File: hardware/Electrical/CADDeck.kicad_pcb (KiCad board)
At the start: 2 copper layers, 129 x 82.1 mm, 26 parts, among them J1 Conn_01x05_Socket, J4 Conn_01x04_Socket, J5 Conn_01x10_Socket, SW1 SW_Push, SW10 SW_Push, SW2 SW_Push, SW3 SW_Push, SW4 SW_Push, SW5 SW_Push, SW6 SW_Push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

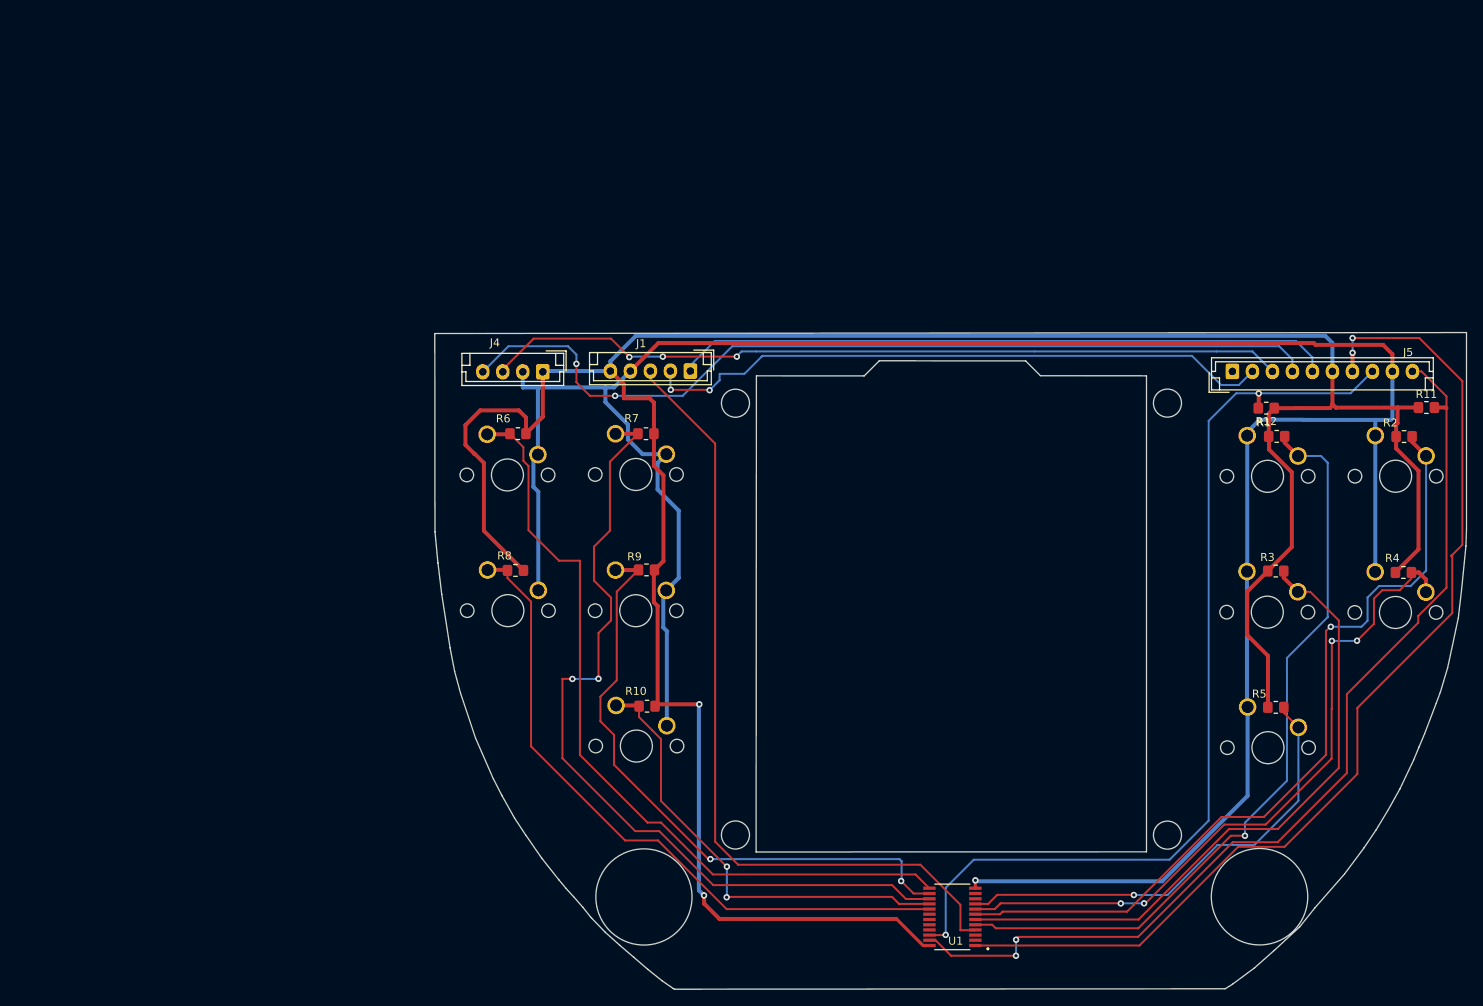
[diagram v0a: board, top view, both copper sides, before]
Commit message: Platine aktualisiert
LED Beleuchtung für Tasten
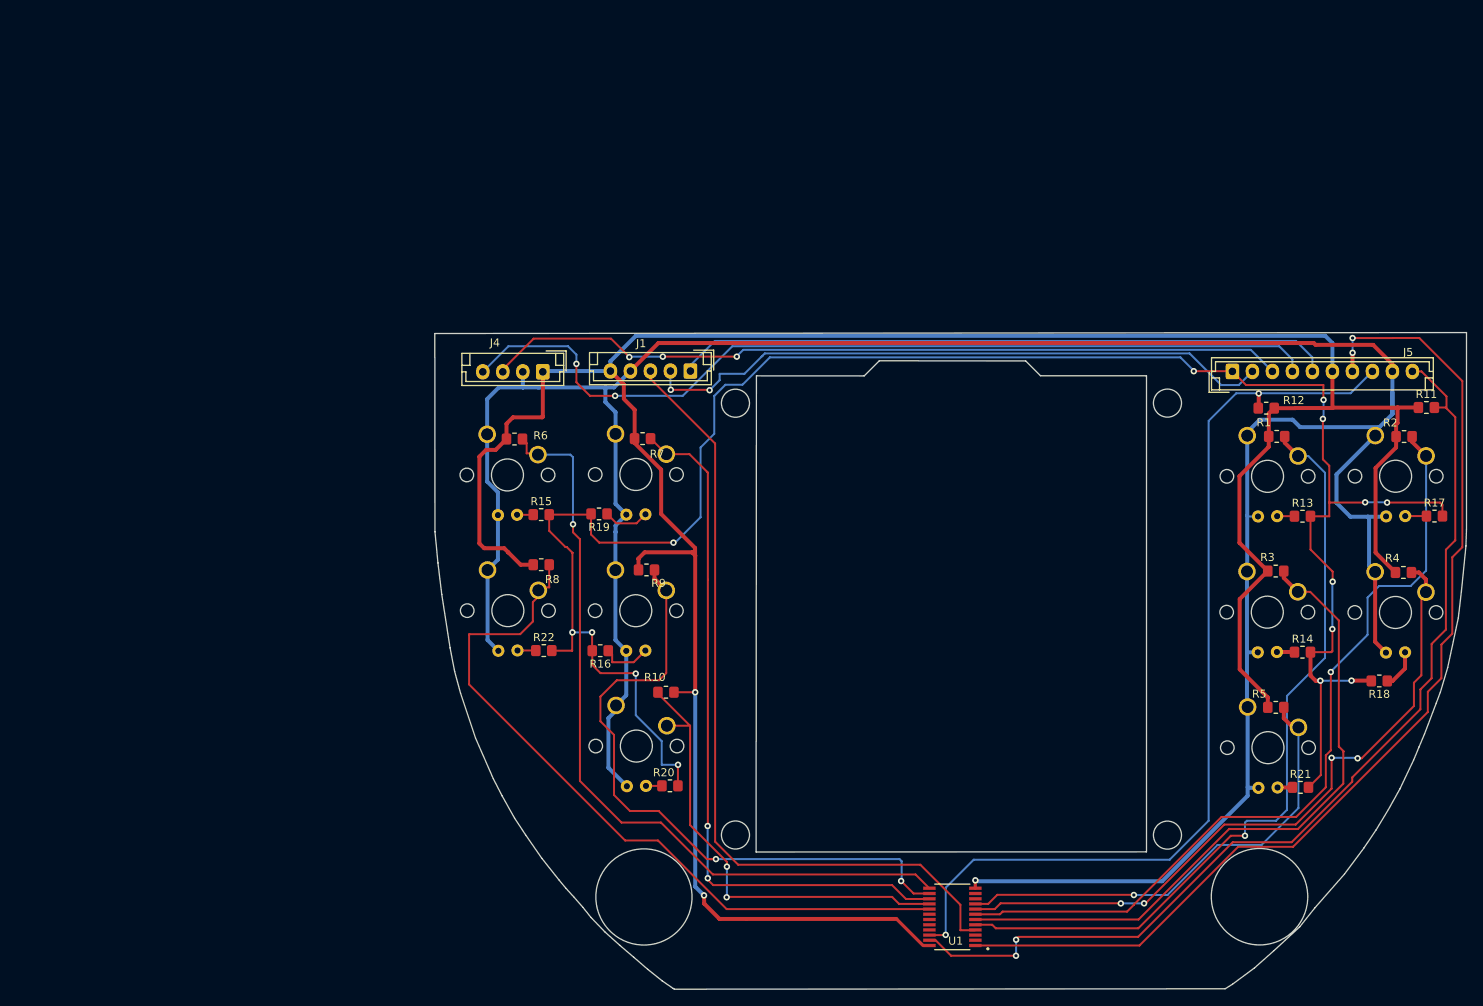
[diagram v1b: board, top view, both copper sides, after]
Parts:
- added R13: 10k, Resistor_SMD:R_0805_2012Metric_Pad1.20x1.40mm_HandSolder, F.Cu at (195.9, 79.6)
- added R14: 10k, Resistor_SMD:R_0805_2012Metric_Pad1.20x1.40mm_HandSolder, F.Cu at (195.9, 96.6)
- added R15: 10k, Resistor_SMD:R_0805_2012Metric_Pad1.20x1.40mm_HandSolder, F.Cu at (100.7, 79.4)
- added R16: 10k, Resistor_SMD:R_0805_2012Metric_Pad1.20x1.40mm_HandSolder, F.Cu at (108.1, 96.4)
- added R17: 10k, Resistor_SMD:R_0805_2012Metric_Pad1.20x1.40mm_HandSolder, F.Cu at (212.4, 79.6)
- added R18: 10k, Resistor_SMD:R_0805_2012Metric_Pad1.20x1.40mm_HandSolder, F.Cu at (205.5, 100.2)
- added R19: 10k, Resistor_SMD:R_0805_2012Metric_Pad1.20x1.40mm_HandSolder, F.Cu at (107.9, 79.3)
- added R20: 10k, Resistor_SMD:R_0805_2012Metric_Pad1.20x1.40mm_HandSolder, F.Cu at (116.8, 113.3)
- added R21: 10k, Resistor_SMD:R_0805_2012Metric_Pad1.20x1.40mm_HandSolder, F.Cu at (195.6, 113.5)
- added R22: 10k, Resistor_SMD:R_0805_2012Metric_Pad1.20x1.40mm_HandSolder, F.Cu at (101.0, 96.4)
- SW1, SW10, SW2, SW3, SW4, SW5, SW6, SW7, SW8, SW9: footprint Button_Switch_Keyboard:SW_Cherry_MX_1.00u_PCB -> Button_MX_LED:SW_Cherry_MX_LED_PCB
- moved R8 3.30 mm to (100.7, 85.7), turned to 0 degrees
- moved R10 2.94 mm to (116.3, 101.6)
- moved R6 0.79 mm to (97.4, 70.0), turned to 0 degrees
- moved R7 0.75 mm to (113.4, 69.9), turned to 0 degrees
- turned R9 to 0 degrees
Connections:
- J5 pad 1: unconnected-(J5-Pin_1-Pad1) -> Net-(J5-Pin_1)
- SW10 pad 1: Net-(U1-P13) -> GND
- SW10 pad 2: GND -> Net-(U1-P13)
- SW3 pad 2: Net-(U1-P02) -> unconnected-(SW3-Pad2)
- SW6 pad 1: Net-(U1-P10) -> GND
- SW6 pad 2: GND -> Net-(U1-P10)
- SW7 pad 1: Net-(U1-P12) -> GND
- SW7 pad 2: GND -> Net-(U1-P12)
- SW8 pad 1: Net-(U1-P14) -> GND
- SW8 pad 2: GND -> Net-(U1-P14)
- SW9 pad 1: Net-(U1-P11) -> GND
- SW9 pad 2: GND -> Net-(U1-P11)
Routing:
- net Net-(J5-Pin_1): track 0.00 -> 250.3 mm, vias 0 -> 14
- net GND: track 321.1 -> 361.6 mm
- net Net-(U1-P12): track 104.9 -> 88.7 mm
- net Net-(U1-P14): track 84.5 -> 92.6 mm
- net Net-(SW9-Anode_+): track 0.00 -> 6.40 mm
- net Net-(U1-P11): track 77.6 -> 83.4 mm
- net Net-(SW7-Anode_+): track 0.00 -> 5.75 mm
- net Net-(SW4-Anode_+): track 0.00 -> 4.89 mm
- net Net-(SW2-Anode_+): track 0.00 -> 2.66 mm
- net Net-(SW8-Anode_+): track 0.00 -> 2.30 mm
- net Net-(SW3-Anode_+): track 0.00 -> 2.21 mm
- net Net-(SW1-Anode_+): track 0.00 -> 2.17 mm
- net Net-(SW6-Anode_+): track 0.00 -> 2.03 mm
- net Net-(SW10-Anode_+): track 0.00 -> 2.00 mm
- net Net-(U1-P02): track 81.7 -> 83.7 mm
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
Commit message: Platine Fehler beseitigt
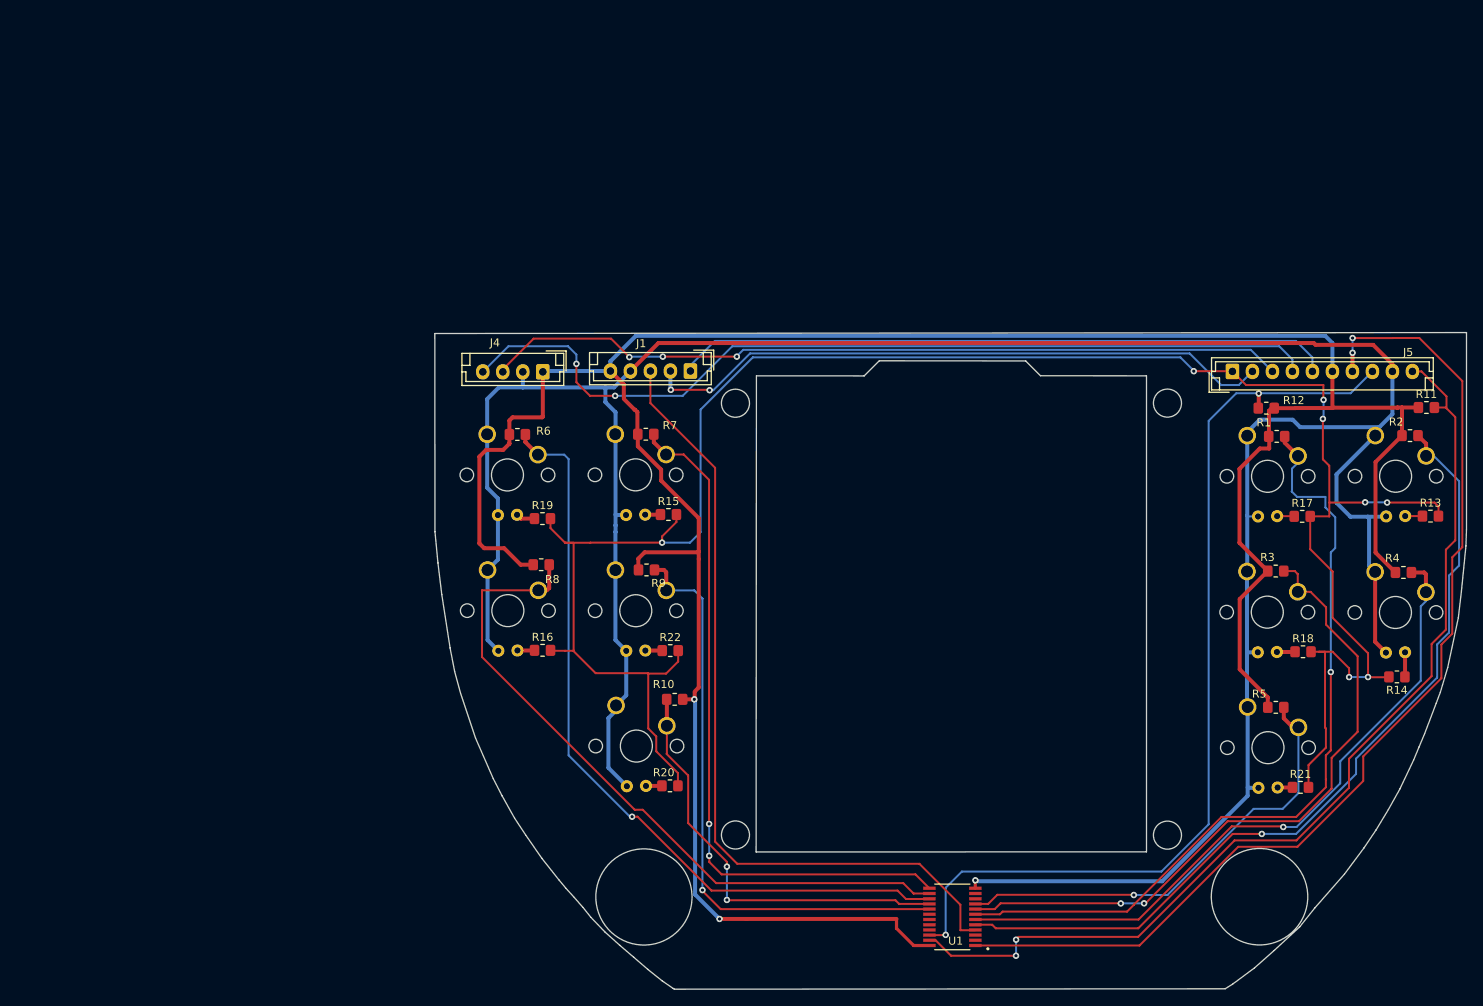
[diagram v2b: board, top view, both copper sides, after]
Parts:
- R13, R14, R15, R16, R17, R18, R19, R20, R21, R22: value 10k -> 100
- moved R17 16.5 mm to (195.8, 79.6)
- moved R13 16.0 mm to (211.9, 79.6)
- moved R15 15.9 mm to (116.6, 79.4)
- moved R22 15.8 mm to (116.8, 96.4)
- moved R14 12.2 mm to (207.7, 99.7), turned to 180 degrees
- moved R18 10.2 mm to (195.9, 96.5), turned to 0 degrees
- moved R16 7.22 mm to (100.9, 96.4), turned to 0 degrees
- moved R19 7.10 mm to (100.9, 79.9), turned to 0 degrees
- moved R10 1.41 mm to (117.4, 102.5)
- moved R2 0.75 mm to (209.3, 69.5)
- moved R7 0.68 mm to (113.8, 69.4)
- moved R6 0.68 mm to (97.7, 69.4)
- moved SW7 0.06 mm to (110.0, 69.3)
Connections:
- R1 pad 2: Net-(U1-P01) -> Net-(U1-P03)
- R13 pad 1: Net-(SW1-Anode_+) -> Net-(SW2-Anode_+)
- R14 pad 1: Net-(SW3-Anode_+) -> Net-(SW4-Anode_+)
- R15 pad 1: Net-(SW6-Anode_+) -> Net-(SW7-Anode_+)
- R16 pad 1: Net-(SW9-Anode_+) -> Net-(SW8-Anode_+)
- R17 pad 1: Net-(SW2-Anode_+) -> Net-(SW1-Anode_+)
- R18 pad 1: Net-(SW4-Anode_+) -> Net-(SW3-Anode_+)
- R19 pad 1: Net-(SW7-Anode_+) -> Net-(SW6-Anode_+)
- R2 pad 2: Net-(U1-P03) -> Net-(U1-P01)
- R21 pad 2: unconnected-(R21-Pad2) -> Net-(J5-Pin_1)
- R22 pad 1: Net-(SW8-Anode_+) -> Net-(SW9-Anode_+)
- R3 pad 2: Net-(U1-P02) -> Net-(U1-P04)
- R4 pad 2: Net-(U1-P04) -> Net-(U1-P02)
- R6 pad 2: Net-(U1-P10) -> Net-(U1-P12)
- R7 pad 2: Net-(U1-P12) -> Net-(U1-P10)
- R8 pad 2: Net-(U1-P14) -> Net-(U1-P11)
- R9 pad 2: Net-(U1-P11) -> Net-(U1-P14)
- SW1 pad 2: Net-(U1-P01) -> Net-(U1-P03)
- SW2 pad 2: Net-(U1-P03) -> Net-(U1-P01)
- SW3 pad 2: unconnected-(SW3-Pad2) -> Net-(U1-P04)
- SW4 pad 2: Net-(U1-P04) -> Net-(U1-P02)
- SW6 pad 2: Net-(U1-P10) -> Net-(U1-P12)
- SW7 pad 2: Net-(U1-P12) -> Net-(U1-P10)
- SW8 pad 2: Net-(U1-P14) -> Net-(U1-P11)
- SW9 pad 2: Net-(U1-P11) -> Net-(U1-P14)
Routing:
- net Net-(U1-P14): track 92.6 -> 73.8 mm, vias 0 -> 1
- net Net-(U1-P10): track 99.8 -> 86.5 mm, vias 1 -> 2
- net Net-(J5-Pin_1): track 250.3 -> 259.8 mm, vias 14 -> 8
- net Net-(U1-P01): track 97.8 -> 106.1 mm
- net Net-(U1-P12): track 88.7 -> 96.8 mm, vias 2 -> 1
- net GND: track 361.6 -> 356.5 mm
- net Net-(U1-P11): track 83.4 -> 87.9 mm, vias 2 -> 0
- net Net-(SW9-Anode_+): track 6.40 -> 2.11 mm
- net Net-(U1-P13): track 57.9 -> 53.8 mm
- net Net-(SW7-Anode_+): track 5.75 -> 1.92 mm
- net Net-(U1-P03): track 102.5 -> 100.1 mm
- net Net-(SW4-Anode_+): track 4.89 -> 3.08 mm
- net Net-(U1-P02): track 83.7 -> 85.2 mm, vias 0 -> 1
- net Net-(U1-P04): track 86.3 -> 84.9 mm, vias 4 -> 2
- net Net-(U1-P05): track 59.1 -> 58.0 mm
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
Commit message: Platine fertig gestellt
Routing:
- net +3.3V: track 345.0 -> 343.3 mm
- net Net-(U1-P14): track 73.8 -> 72.9 mm
- net Net-(U1-P13): track 53.8 -> 53.3 mm
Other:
- outline, holes or cut-outs redrawn

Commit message: Alle Platinen fertiggestellt
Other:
- board text added: "AFUDirk CADDeck 10 Buttons"
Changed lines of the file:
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@@
   (gr_line (start 189.86 136.06) (end 187.11 138.1)
     (stroke (width 0.1) (type default)) (layer "Edge.Cuts"))
+  (gr_text "AFUDirk\nCADDeck 10 Buttons" (at 122.58 136.713) (layer "F.Cu")
+    (effects (font (size 2 2) (thickness 0.4) bold) (justify left bottom))
+  )
   (segment (start 119.885 102.442) (end 119.885 101.665) (width 0.5) (layer "F.Cu") (net 1))
   (segment (start 208.274 66.01) (end 210.35 66.01) (width 0.5) (layer "F.Cu") (net 1))
